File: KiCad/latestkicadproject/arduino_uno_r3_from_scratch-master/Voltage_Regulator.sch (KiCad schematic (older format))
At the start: 8 parts, among them CON1 BARREL_JACK, U1 LD1117S50TR

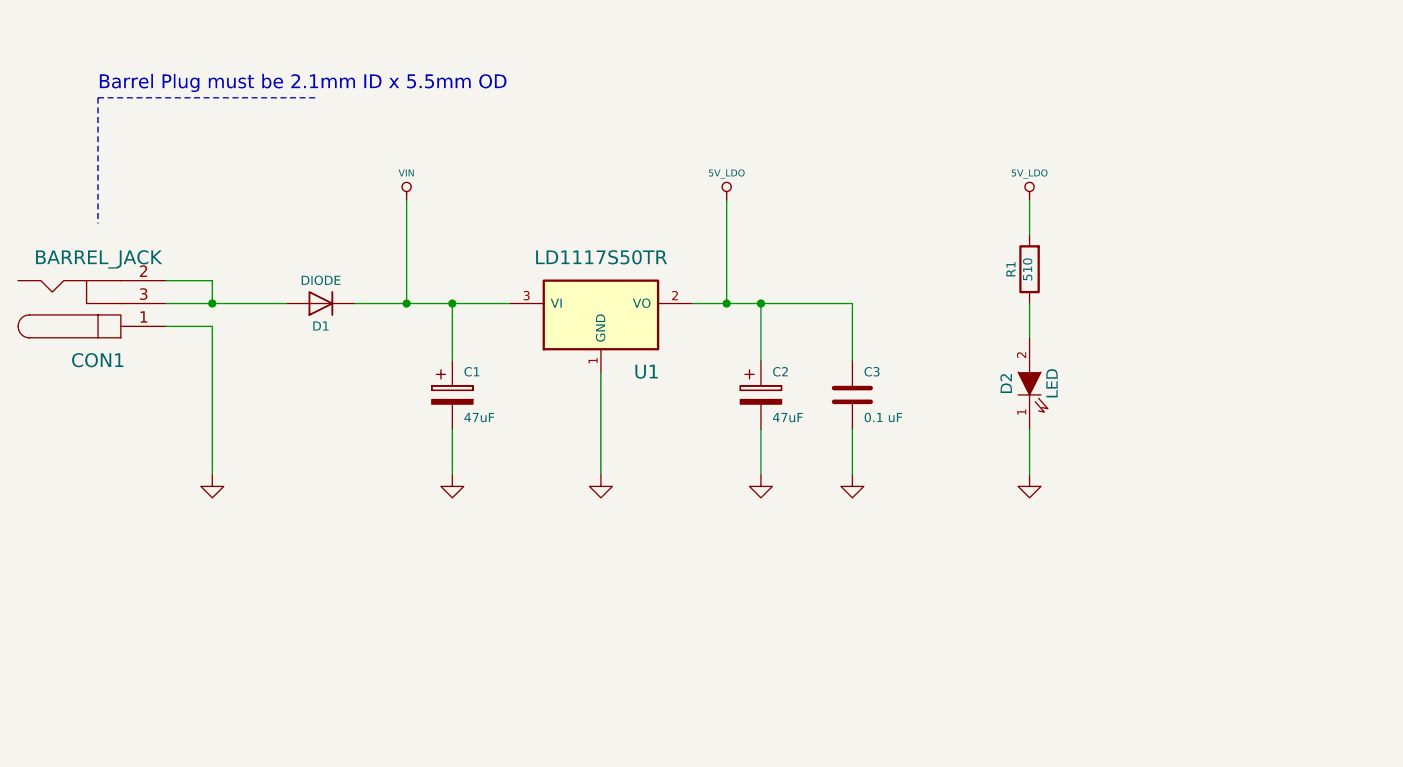
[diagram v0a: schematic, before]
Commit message: 28feb
Aanpassing KiCad+deel footprints
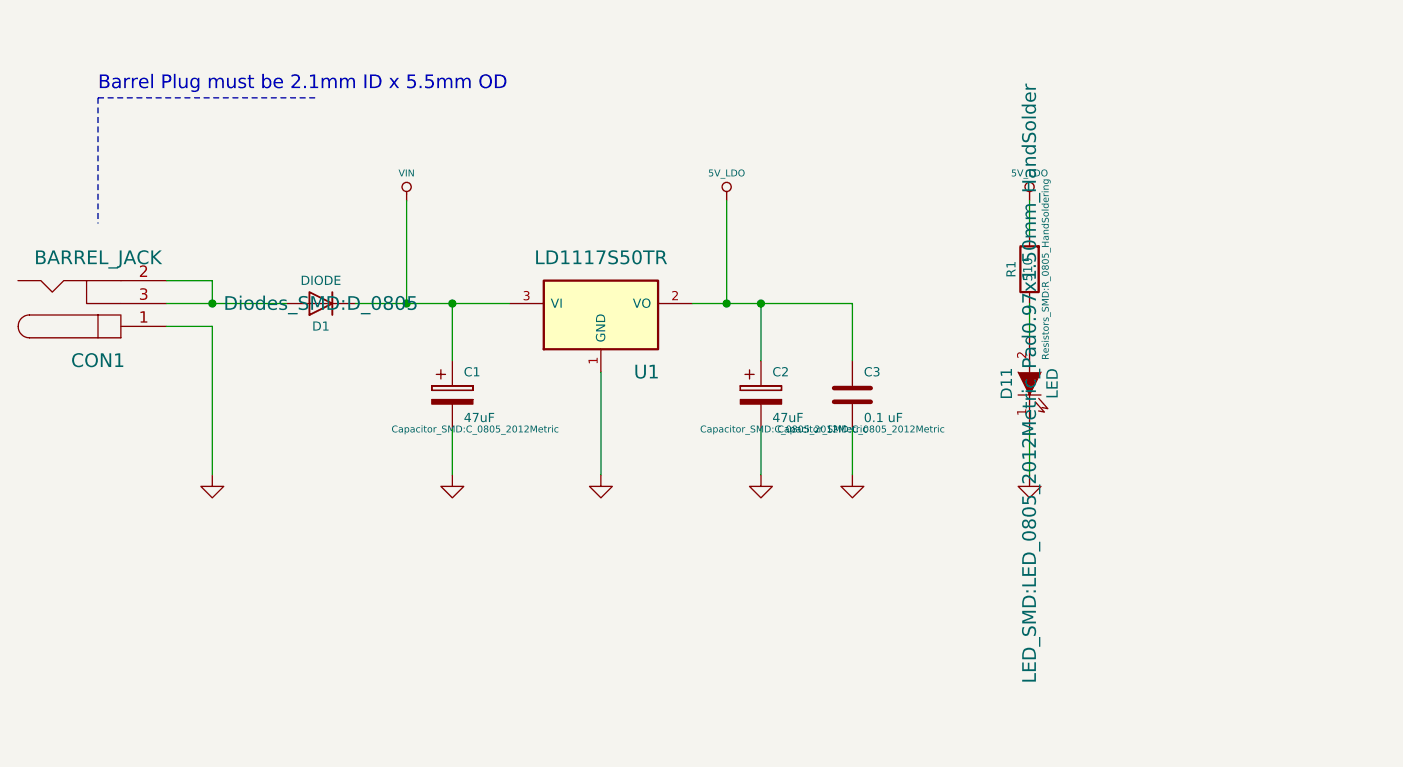
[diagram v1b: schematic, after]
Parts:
- C1, C2, C3: footprint ~ -> Capacitor_SMD:C_0805_2012Metric
- CON1: footprint ~ -> (none)
- D1: footprint ~ -> Diodes_SMD:D_0805
- D11: renamed from D2; footprint ~ -> LED_SMD:LED_0805_2012Metric_Pad0.97x1.50mm_HandSolder
- R1: footprint ~ -> Resistors_SMD:R_0805_HandSoldering
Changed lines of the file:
@@
 F 0 "D1" H 4700 3875 40  0000 C CNN
 F 1 "DIODE" H 4700 3675 40  0000 C CNN
-F 2 "~" H 4700 3775 60  0000 C CNN
+F 2 "Diodes_SMD:D_0805" H 4700 3775 60  0000 C CNN
 F 3 "http://www.onsemi.com/pub_link/Collateral/MRA4003T3-D.PDF" H 4700 3775 60  0001 C CNN
 F 4 "1A, 1000V, SILICON, SIGNAL DIODE, ROHS COMPLIANT, COMPACT, PLASTIC, CASE 403D-02, SMA, 2 PIN" H 4700 3775 60  0001 C CNN "Characteristics"
@@
 F 0 "C1" H 5325 4275 40  0000 L CNN
 F 1 "47uF" H 5325 4075 40  0000 L CNN
-F 2 "~" H 5375 4025 30  0000 C CNN
+F 2 "Capacitor_SMD:C_0805_2012Metric" H 5375 4025 30  0000 C CNN
 F 3 "http://images.ihscontent.net/vipimages/VipMasterIC/IC/BEYS/BEYSS04513/BEYSS04513-1.pdf" H 5275 4175 300 0001 C CNN
 F 4 "CAPACITOR, ALUMINUM ELECTROLYTIC, NON SOLID, POLARIZED, 50 V, 47 uF, SURFACE MOUNT, 3131, CHIP, ROHS COMPLIANT" H 5275 4175 60  0001 C CNN "Characteristics"
@@
 F 0 "C3" H 7075 4275 40  0000 L CNN
 F 1 "0.1 uF" H 7075 4075 40  0000 L CNN
-F 2 "~" H 7063 4025 30  0000 C CNN
+F 2 "Capacitor_SMD:C_0805_2012Metric" H 7063 4025 30  0000 C CNN
 F 3 "http://images.ihscontent.net/vipimages/VipMasterIC/IC/KEME/KEMES10043/KEMES10043-1.pdf" H 7025 4175 60  0001 C CNN
 F 4 "CAPACITOR, CERAMIC, MULTILAYER, 100 V, X7R, 0.1 uF, SURFACE MOUNT, 0805, CHIP, ROHS COMPLIANT" H 7025 4175 60  0001 C CNN "Characteristics"
@@
 F 0 "CON1" H 3725 4025 60  0000 C CNN
 F 1 "BARREL_JACK" H 3725 3575 60  0000 C CNN
-F 2 "~" H 3725 3775 60  0000 C CNN
+F 2 "" H 3725 3775 60  0000 C CNN
 F 3 "http://katalog.we-online.de/em/datasheet/6941xx106102.pdf" H 3725 3775 60  0001 C CNN
 F 4 "CONN PWR JACK DC RA SMD	" H 3725 3775 60  0001 C CNN "Characteristics"
@@
 F 0 "C2" H 6675 4275 40  0000 L CNN
 F 1 "47uF" H 6675 4075 40  0000 L CNN
-F 2 "~" H 6725 4025 30  0000 C CNN
+F 2 "Capacitor_SMD:C_0805_2012Metric" H 6725 4025 30  0000 C CNN
 F 3 "http://images.ihscontent.net/vipimages/VipMasterIC/IC/BEYS/BEYSS04513/BEYSS04513-1.pdf" H 6625 4175 300 0001 C CNN
 F 4 "CAPACITOR, ALUMINUM ELECTROLYTIC, NON SOLID, POLARIZED, 50 V, 47 uF, SURFACE MOUNT, 3131, CHIP, ROHS COMPLIANT" H 6625 4175 60  0001 C CNN "Characteristics"
@@
 F 0 "R1" V 7880 3625 40  0000 C CNN
 F 1 "510" V 7807 3626 40  0000 C CNN
-F 2 "~" V 7730 3625 30  0000 C CNN
+F 2 "Resistors_SMD:R_0805_HandSoldering" V 7730 3625 30  0000 C CNN
 F 3 "http://www.yageo.com/pdf/Pu-RC0805_51_PbFree_L_2.pdf" H 7800 3625 30  0001 C CNN
 F 4 "RESISTOR, METAL GLAZE/THICK FILM, 0.125W, 1%, 100ppm, 510ohm, SURFACE MOUNT, 0805" H 7800 3625 60  0001 C CNN "Characteristics"
@@
 $EndComp
 $Comp
-L LED-RESCUE-Arduino_Uno_R3_From_Scratch D2
+L LED-RESCUE-Arduino_Uno_R3_From_Scratch D11
 U 1 1 55D1FC7B
 P 7800 4125
-F 0 "D2" H 7800 4225 50  0000 C CNN
+F 0 "D11" H 7800 4225 50  0000 C CNN
 F 1 "LED" H 7800 4025 50  0000 C CNN
-F 2 "~" H 7800 4125 60  0000 C CNN
+F 2 "LED_SMD:LED_0805_2012Metric_Pad0.97x1.50mm_HandSolder" H 7800 4125 60  0000 C CNN
 F 3 "http://www.osram-os.com/Graphics/XPic9/00078860_0.pdf" H 7800 4125 60  0001 C CNN
 F 4 "LED CHIPLED 570NM GREEN" H 7800 4125 60  0001 C CNN "Characteristics"
@@
 F 0 "U1" H 6125 3575 60  0000 C CNN
 F 1 "LD1117S50TR" H 5925 4075 60  0000 C CNN
-F 2 "" H 5925 3825 60  0000 C CNN
+F 2 "" H 5925 3825 60  0001 C CNN
 F 3 "http://www.st.com/st-web-ui/static/active/en/resource/technical/document/datasheet/CD00000544.pdf" H 5925 3825 60  0001 C CNN
 F 4 "5 V FIXED POSITIVE LDO REGULATOR, 1.2 V DROPOUT, PDSO3, ROHS COMPLIANT, SOT-223, 4 PIN" H 5925 3825 60  0001 C CNN "Characteristics"

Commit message: Toevoegen footprints Kicad
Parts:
- CON1: footprint (none) -> Connectors:BARREL_JACK
- U1: footprint (none) -> LD1117S50TR:LD1117S50TR
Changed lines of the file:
@@
 F 0 "CON1" H 3725 4025 60  0000 C CNN
 F 1 "BARREL_JACK" H 3725 3575 60  0000 C CNN
-F 2 "" H 3725 3775 60  0000 C CNN
+F 2 "Connectors:BARREL_JACK" H 3725 3775 60  0001 C CNN
 F 3 "http://katalog.we-online.de/em/datasheet/6941xx106102.pdf" H 3725 3775 60  0001 C CNN
 F 4 "CONN PWR JACK DC RA SMD	" H 3725 3775 60  0001 C CNN "Characteristics"
@@
 F 0 "U1" H 6125 3575 60  0000 C CNN
 F 1 "LD1117S50TR" H 5925 4075 60  0000 C CNN
-F 2 "" H 5925 3825 60  0001 C CNN
+F 2 "LD1117S50TR:LD1117S50TR" H 5925 3825 60  0001 C CNN
 F 3 "http://www.st.com/st-web-ui/static/active/en/resource/technical/document/datasheet/CD00000544.pdf" H 5925 3825 60  0001 C CNN
 F 4 "5 V FIXED POSITIVE LDO REGULATOR, 1.2 V DROPOUT, PDSO3, ROHS COMPLIANT, SOT-223, 4 PIN" H 5925 3825 60  0001 C CNN "Characteristics"

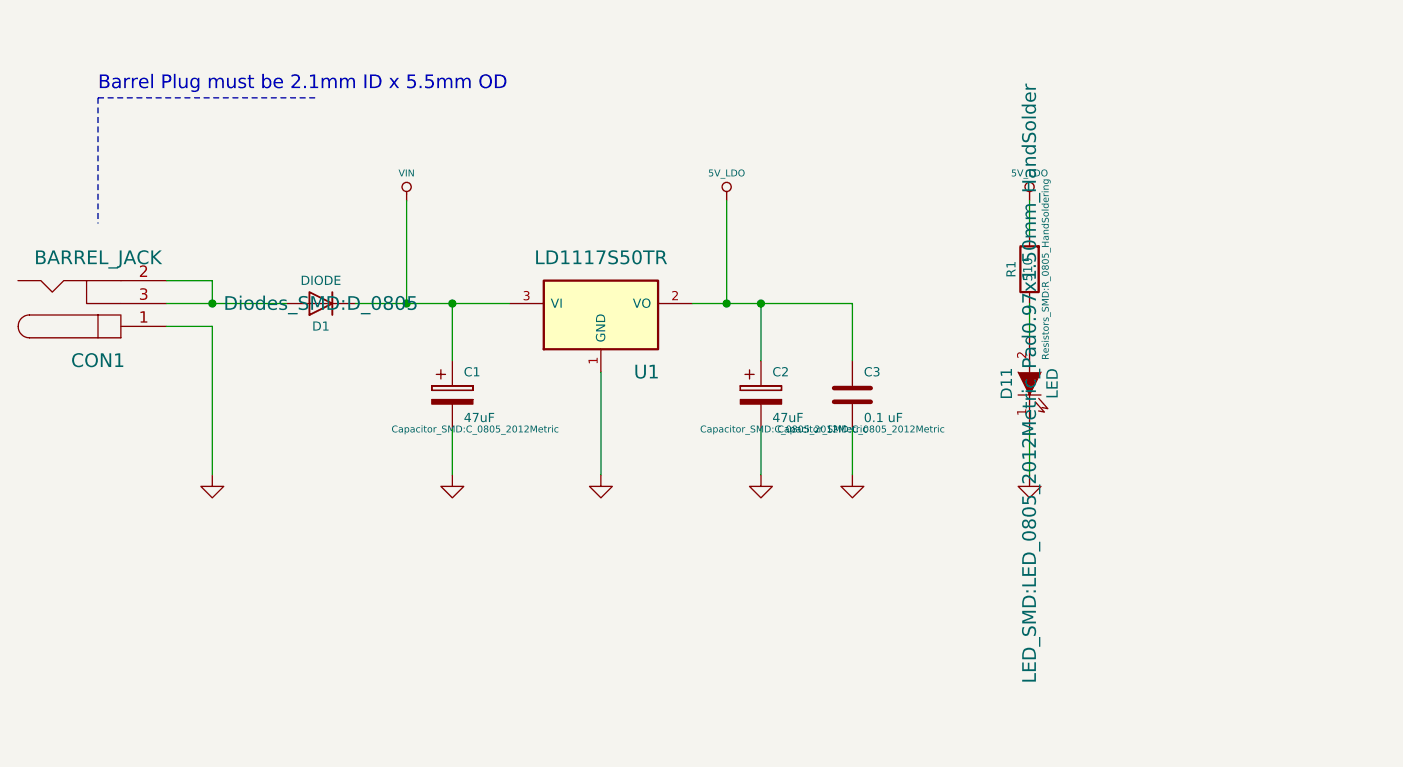
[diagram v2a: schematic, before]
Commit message: Aanpassing KiCad PCB ontwerp + footprints
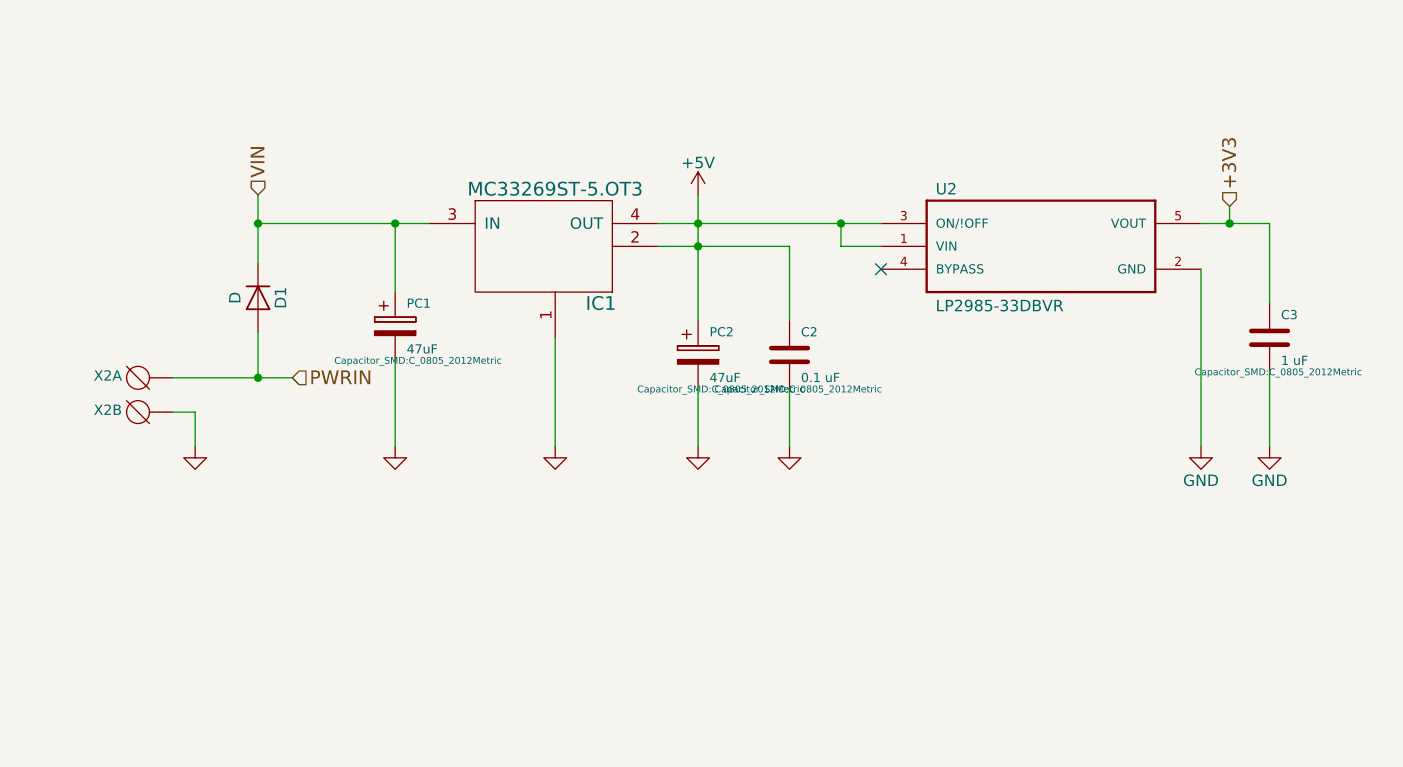
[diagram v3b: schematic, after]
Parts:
- removed CON1: BARREL_JACK, Connectors:BARREL_JACK, symbol BARREL_JACK-RESCUE-Arduino_Uno_R3_From_Scratch
- removed D11: LED, LED_SMD:LED_0805_2012Metric_Pad0.97x1.50mm_HandSolder, symbol LED-RESCUE-Arduino_Uno_R3_From_Scratch
- removed R1: 510, Resistors_SMD:R_0805_HandSoldering, symbol R
- removed U1: LD1117S50TR, LD1117S50TR:LD1117S50TR, symbol LD1117S50TR-RESCUE-Arduino_Uno_R3_From_Scratch
- added C3: 1 uF, Capacitor_SMD:C_0805_2012Metric, symbol C
- added IC1: MC33269ST-5.OT3, MC33269ST-3.3T3G:SOT230P700X175-4N, symbol MC33269ST-5.OT3
- added U2: LP2985-33DBVR, LP2985-33DBVR:SOT95P280X145-5N, symbol LP2985-33DBVR
- added X2: DG3XX-02-3.5, degson:degson-DG350-3.5-02P, symbol DG3XX-02-3.5
- D1: value DIODE -> D; Characteristics 1A, 1000V, SILICON, SIGNAL DIODE, ROHS COMPLIANT, COMPACT, 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 -> (none); Critical N -> (none); Description Reverse Voltage Protection Diode -> (none); MFN ON Semi -> (none); MFP MRA4007T3G -> (none); Package ID R-PDSO-J2 -> (none); Source ANY -> (none); Subsystem Voltage_Reg -> (none)
- renumbered C3 to C2, C1 to PC1, C2 to PC2
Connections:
- net VIN: now reaches D1.1 (K), PC1.1
- net VIN: now also IC1.3 (IN)
- net PWRIN: now reaches D1.2 (A)
- net PWRIN: now also X2.1 (KL)
- net 5V_LDO renamed +5V
- net +5V: now also IC1.2, IC1.4 (OUT), U2.1 (VIN), U2.3 (ON/!OFF)
- new net +3V3: C3.1, U2.5 (VOUT)
- new net GND: C3.2, U2.2 (GND)
- no-connect marks 0 -> 1
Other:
- note removed: "Barrel Plug must be 2.1mm ID x 5.5mm OD"
- moved on the sheet: C2, PC1, PC2

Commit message: pcb routing
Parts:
- D1: footprint Diodes_SMD:D_0805 -> Diodes_SMD:D_MicroMELF_Hadsoldering
- PC1, PC2: footprint Capacitor_SMD:C_0805_2012Metric -> Capacitors_SMD:CP_Elec_4x5.3
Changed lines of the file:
@@
 LIBS:LP2985-33DBVR
 LIBS:degson
+LIBS:PHT6NQ10T_135
 EELAYER 25 0
 EELAYER END
@@
 F 0 "PC1" H 5075 3975 40  0000 L CNN
 F 1 "47uF" H 5075 3775 40  0000 L CNN
-F 2 "Capacitor_SMD:C_0805_2012Metric" H 5125 3725 30  0000 C CNN
+F 2 "Capacitors_SMD:CP_Elec_4x5.3" H 5125 3725 30  0000 C CNN
 F 3 "http://images.ihscontent.net/vipimages/VipMasterIC/IC/BEYS/BEYSS04513/BEYSS04513-1.pdf" H 5025 3875 300 0001 C CNN
 F 4 "CAPACITOR, ALUMINUM ELECTROLYTIC, NON SOLID, POLARIZED, 50 V, 47 uF, SURFACE MOUNT, 3131, CHIP, ROHS COMPLIANT" H 5025 3875 60  0001 C CNN "Characteristics"
@@
 F 0 "PC2" H 6400 4100 40  0000 L CNN
 F 1 "47uF" H 6400 3900 40  0000 L CNN
-F 2 "Capacitor_SMD:C_0805_2012Metric" H 6450 3850 30  0000 C CNN
+F 2 "Capacitors_SMD:CP_Elec_4x5.3" H 6450 3850 30  0000 C CNN
 F 3 "http://images.ihscontent.net/vipimages/VipMasterIC/IC/BEYS/BEYSS04513/BEYSS04513-1.pdf" H 6350 4000 300 0001 C CNN
 F 4 "CAPACITOR, ALUMINUM ELECTROLYTIC, NON SOLID, POLARIZED, 50 V, 47 uF, SURFACE MOUNT, 3131, CHIP, ROHS COMPLIANT" H 6350 4000 60  0001 C CNN "Characteristics"
@@
 F 0 "D1" H 4425 3850 50  0000 C CNN
 F 1 "D" H 4425 3650 50  0000 C CNN
-F 2 "Diodes_SMD:D_0805" H 4425 3750 50  0001 C CNN
+F 2 "Diodes_SMD:D_MicroMELF_Hadsoldering" H 4425 3750 50  0001 C CNN
 F 3 "" H 4425 3750 50  0001 C CNN
 	1    4425 3750

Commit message: PCB routing v1
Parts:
- removed U2: LP2985-33DBVR, LP2985-33DBVR:SOT95P280X145-5N, symbol LP2985-33DBVR
- added IC2: MC33269ST-5.OT3, MC33269ST-3.3T3G:SOT230P700X175-4N, symbol MC33269ST-5.OT3
- C2, C3: footprint Capacitor_SMD:C_0805_2012Metric -> Capacitors_SMD:C_0805
- PC1, PC2: footprint Capacitors_SMD:CP_Elec_4x5.3 -> Capacitors_SMD:CP_Elec_6.3x5.3
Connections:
- net +3V3: now also IC2.2, IC2.4 (OUT)
- net +5V: now also IC2.3 (IN)
- net GND: now also IC2.1
- no-connect marks 1 -> 0
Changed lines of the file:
@@
 LIBS:degson
 LIBS:PHT6NQ10T_135
+LIBS:L298P
 EELAYER 25 0
 EELAYER END
@@
 F 0 "PC1" H 5075 3975 40  0000 L CNN
 F 1 "47uF" H 5075 3775 40  0000 L CNN
-F 2 "Capacitors_SMD:CP_Elec_4x5.3" H 5125 3725 30  0000 C CNN
+F 2 "Capacitors_SMD:CP_Elec_6.3x5.3" H 5125 3725 30  0000 C CNN
 F 3 "http://images.ihscontent.net/vipimages/VipMasterIC/IC/BEYS/BEYSS04513/BEYSS04513-1.pdf" H 5025 3875 300 0001 C CNN
 F 4 "CAPACITOR, ALUMINUM ELECTROLYTIC, NON SOLID, POLARIZED, 50 V, 47 uF, SURFACE MOUNT, 3131, CHIP, ROHS COMPLIANT" H 5025 3875 60  0001 C CNN "Characteristics"
@@
 F 0 "C2" H 6800 4100 40  0000 L CNN
 F 1 "0.1 uF" H 6800 3900 40  0000 L CNN
-F 2 "Capacitor_SMD:C_0805_2012Metric" H 6788 3850 30  0000 C CNN
+F 2 "Capacitors_SMD:C_0805" H 6788 3850 30  0000 C CNN
 F 3 "http://images.ihscontent.net/vipimages/VipMasterIC/IC/KEME/KEMES10043/KEMES10043-1.pdf" H 6750 4000 60  0001 C CNN
 F 4 "CAPACITOR, CERAMIC, MULTILAYER, 100 V, X7R, 0.1 uF, SURFACE MOUNT, 0805, CHIP, ROHS COMPLIANT" H 6750 4000 60  0001 C CNN "Characteristics"
@@
 F 0 "PC2" H 6400 4100 40  0000 L CNN
 F 1 "47uF" H 6400 3900 40  0000 L CNN
-F 2 "Capacitors_SMD:CP_Elec_4x5.3" H 6450 3850 30  0000 C CNN
+F 2 "Capacitors_SMD:CP_Elec_6.3x5.3" H 6450 3850 30  0000 C CNN
 F 3 "http://images.ihscontent.net/vipimages/VipMasterIC/IC/BEYS/BEYSS04513/BEYSS04513-1.pdf" H 6350 4000 300 0001 C CNN
 F 4 "CAPACITOR, ALUMINUM ELECTROLYTIC, NON SOLID, POLARIZED, 50 V, 47 uF, SURFACE MOUNT, 3131, CHIP, ROHS COMPLIANT" H 6350 4000 60  0001 C CNN "Characteristics"
@@
 Wire Wire Line
 	6750 3525 6750 3850
-Connection ~ 6975 3425
 $Comp
 L GND #PWR06
 U 1 1 5AA01DB9
-P 8550 4400
-F 0 "#PWR06" H 8550 4150 50  0001 C CNN
-F 1 "GND" H 8550 4250 50  0000 C CNN
-F 2 "" H 8550 4400 50  0001 C CNN
-F 3 "" H 8550 4400 50  0001 C CNN
-	1    8550 4400
-	1    0    0    -1
-$EndComp
-Wire Wire Line
-	8550 3625 8550 4400
+P 7700 4400
+F 0 "#PWR06" H 7700 4150 50  0001 C CNN
+F 1 "GND" H 7700 4250 50  0000 C CNN
+F 2 "" H 7700 4400 50  0001 C CNN
+F 3 "" H 7700 4400 50  0001 C CNN
+	1    7700 4400
+	1    0    0    -1
+$EndComp
 $Comp
 L C C3
@@
 F 0 "C3" H 8900 4025 40  0000 L CNN
 F 1 "1 uF" H 8900 3825 40  0000 L CNN
-F 2 "Capacitor_SMD:C_0805_2012Metric" H 8888 3775 30  0000 C CNN
+F 2 "Capacitors_SMD:C_0805" H 8888 3775 30  0000 C CNN
 F 3 "http://images.ihscontent.net/vipimages/VipMasterIC/IC/KEME/KEMES10043/KEMES10043-1.pdf" H 8850 3925 60  0001 C CNN
 F 4 "CAPACITOR, CERAMIC, MULTILAYER, 100 V, X7R, 0.1 uF, SURFACE MOUNT, 0805, CHIP, ROHS COMPLIANT" H 8850 3925 60  0001 C CNN "Characteristics"
@@
 $EndComp
 Wire Wire Line
-	8550 3425 8850 3425
+	8150 3425 8850 3425
 Wire Wire Line
 	8850 3425 8850 3775
@@
 Text HLabel 8675 3350 1    60   Input ~ 0
 +3V3
-Wire Wire Line
-	6975 3425 6975 3525
-Wire Wire Line
-	6975 3525 7150 3525
-$Comp
-L LP2985-33DBVR U2
-U 1 1 5AA06B18
-P 7850 3525
-F 0 "U2" H 7389 3746 50  0000 L BNN
-F 1 "LP2985-33DBVR" H 7389 3235 50  0000 L BNN
-F 2 "LP2985-33DBVR:SOT95P280X145-5N" H 7850 3525 50  0001 L BNN
-F 3 "Good" H 7850 3525 50  0001 L BNN
-F 4 "Texas Instruments" H 7850 3525 50  0001 L BNN "Field4"
-F 5 "IC REG LINEAR 3.3V 150MA SOT23-5" H 7850 3525 50  0001 L BNN "Field5"
-F 6 "0.34 USD" H 7850 3525 50  0001 L BNN "Field6"
-F 7 "SOT-23-5 Texas Instruments" H 7850 3525 50  0001 L BNN "Field7"
-F 8 "LP2985-33DBVR" H 7850 3525 50  0001 L BNN "Field8"
-	1    7850 3525
-	1    0    0    -1
-$EndComp
-NoConn ~ 7150 3625
 Wire Wire Line
 	4150 4250 4150 4400
@@
 	-1   0    0    1
 $EndComp
+$Comp
+L MC33269ST-5.OT3 IC2
+U 1 1 5AB3045E
+P 7700 3525
+F 0 "IC2" H 7900 3275 60  0000 C CNN
+F 1 "MC33269ST-5.OT3" H 7700 3775 60  0000 C CNN
+F 2 "MC33269ST-3.3T3G:SOT230P700X175-4N" H 7350 3425 60  0001 C CNN
+F 3 "" H 7350 3425 60  0001 C CNN
+	1    7700 3525
+	1    0    0    -1
+$EndComp
+Wire Wire Line
+	7700 3925 7700 4400
+Wire Wire Line
+	8150 3525 8250 3525
+Wire Wire Line
+	8250 3525 8250 3425
+Connection ~ 8250 3425
 $EndSCHEMATC
